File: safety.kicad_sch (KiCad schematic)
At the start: 12 parts, among them J5 Screw_Terminal_01x02, J7 Screw_Terminal_01x02, SW2 SW_DIP_x03, U11 74LVC2G08, U16 74LVC1G175, U17 74HC123, Y2 SG-3031CM

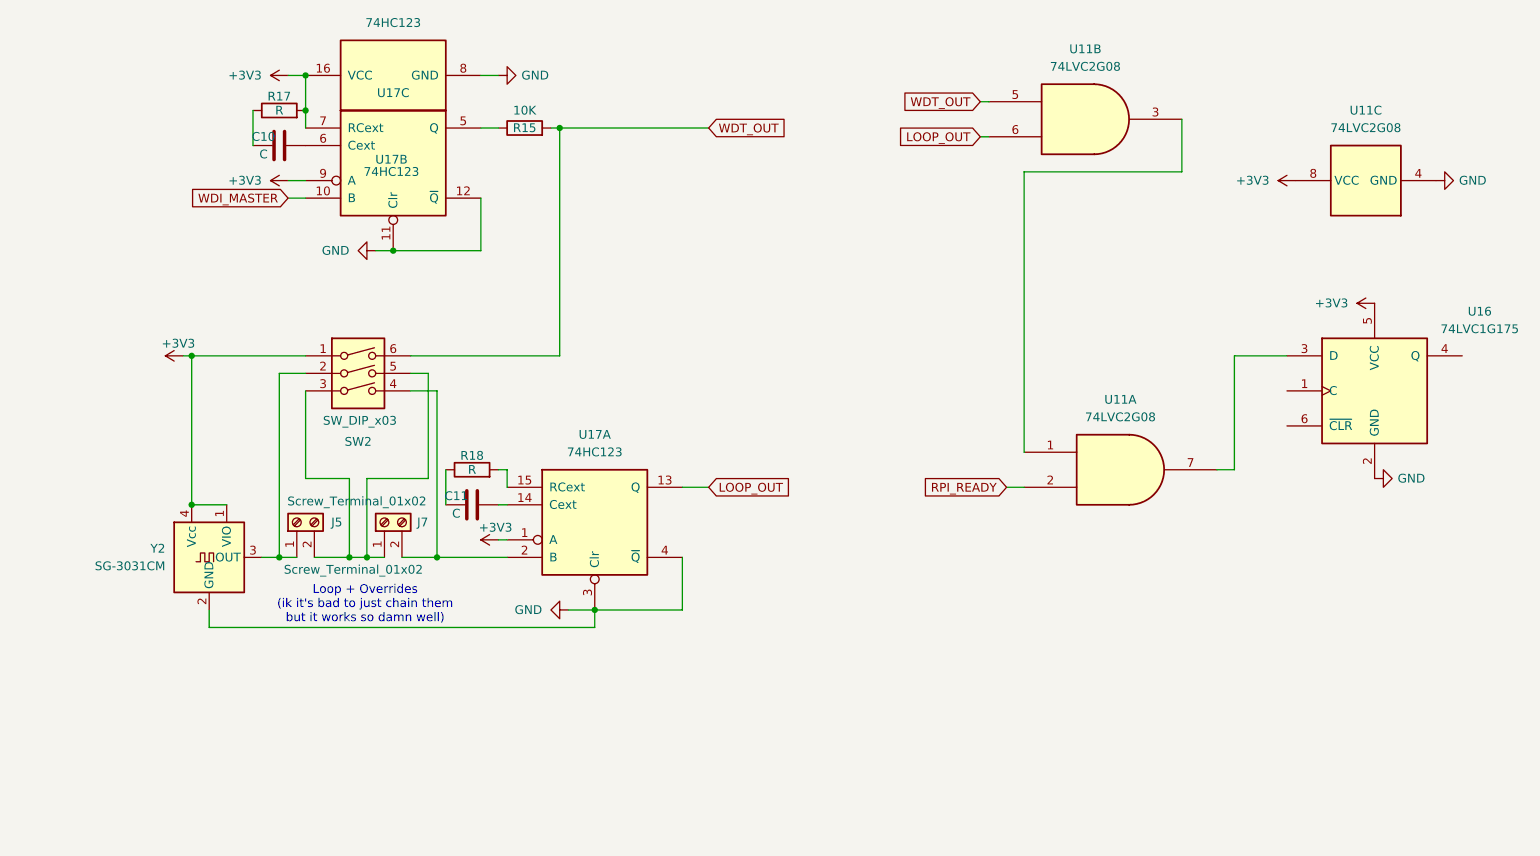
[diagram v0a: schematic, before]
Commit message: Separate safety circuitry, minor schematic changes in main page
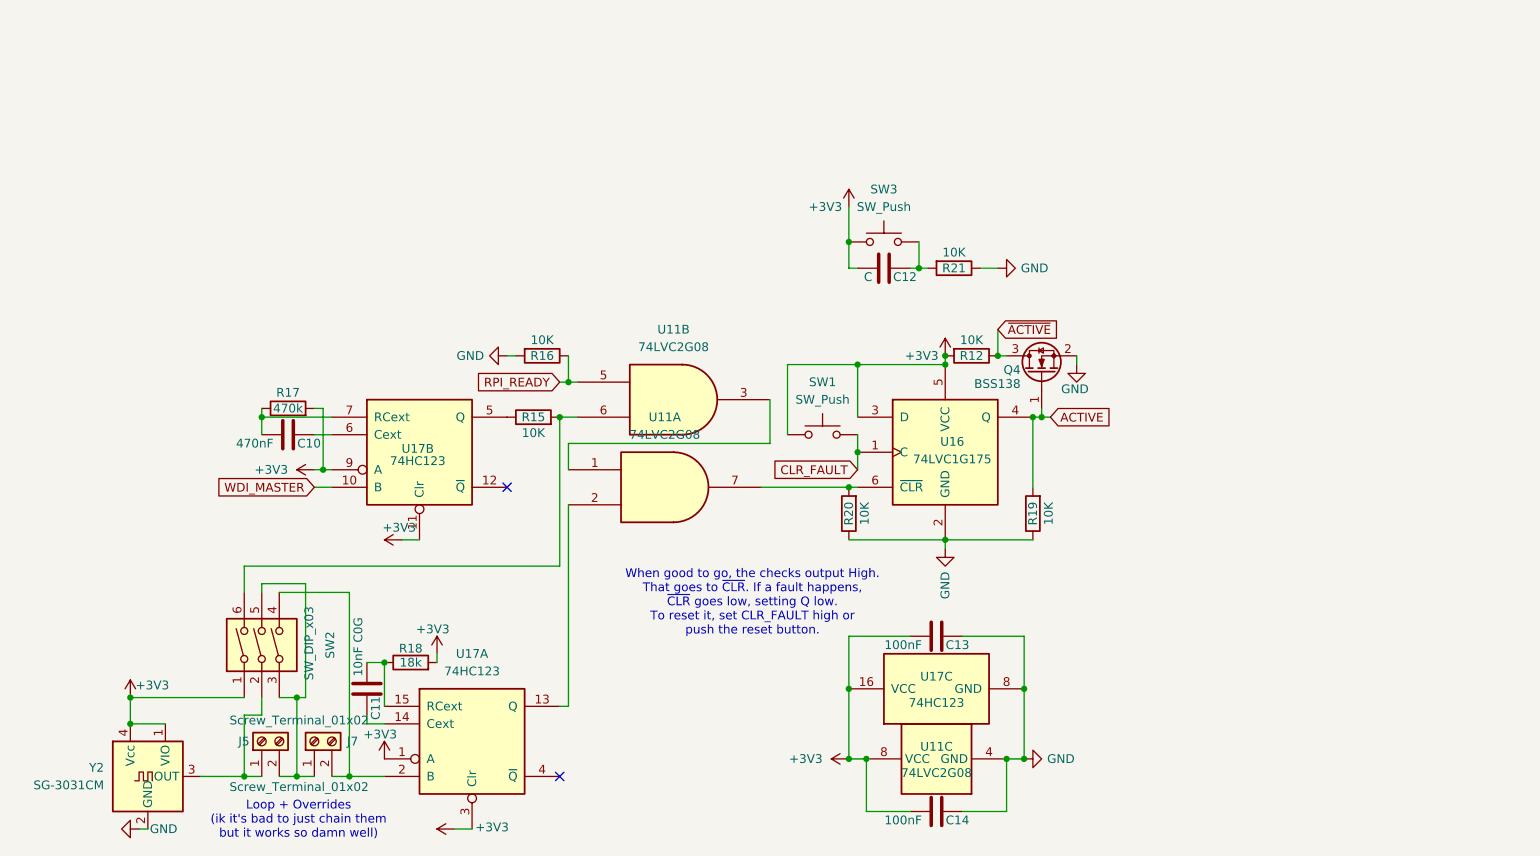
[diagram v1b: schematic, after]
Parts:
- added C12: C, symbol Device:C
- added C13, C14: 100nF, symbol Device:C
- added Q4: BSS138, Package_TO_SOT_SMD:SOT-23, symbol Transistor_FET:BSS138
- added R12, R16, R19, R20, R21: 10K, Resistor_SMD:R_0805_2012Metric_Pad1.20x1.40mm_HandSolder, symbol Device:R
- added SW1, SW3: SW_Push, Button_Switch_SMD:SW_Push_1P1T_NO_CK_KMR2, symbol Switch:SW_Push
- C10: value C -> 470nF
- C11: value C -> 10nF C0G
- R17: value R -> 470k
- R18: value R -> 18k
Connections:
- net +3V3: now also R18.2, U16.3 (D), U17.11 (Clr), U17.3 (Clr), C12.2, C13.2, C14.2, R12.2, SW1.1, SW3.1; no longer U17.7 (RCext)
- net GND: now also C13.1, C14.1, Q4.2 (S), R16.2, R19.1, R20.1, R21.1; no longer U17.11 (Clr), U17.12 (~{Q}), U17.3 (Clr), U17.4 (~{Q})
- net RPI_READY: now also U11.5, R16.1; no longer U11.2
- net at U11.7: now also U16.6 (~{CLR}), R20.2; no longer U16.3 (D)
- net at C11.2, R18.1: now also U17.15 (RCext)
- net at C10.2, R17.1: now also U17.7 (RCext)
- net CLR_FAULT: now reaches U16.1 (C)
- net CLR_FAULT: now also SW1.2
- net ACTIVE: now reaches U16.4 (Q)
- net ACTIVE: now also Q4.1 (G), R19.2
- net LOOP_OUT: no longer names the net of U17.13 (Q)
- net LOOP_OUT: now also U11.2; no longer U11.6
- net WDT_OUT: no longer names the net of R15.2, SW2.6
- net WDT_OUT: now also U11.6; no longer U11.5
- new net: C12.1, R21.2, SW3.2
- new net ~{ACTIVE}: Q4.3 (D), R12.1
- no-connect marks 0 -> 2
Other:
- note added: "When good to go, the checks output High. That goes to ~{CLR}. If a fault happens, ~{CLR} goes low, setting Q low. To reset it, set CLR_FAULT high or push the reset button."
- moved on the sheet: C10, C11, J5, J7, R15, R17, R18, SW2, U11A, U11B, U11C, U16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

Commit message: Started on design, minor touch ups on schematic
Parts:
- removed SW1: SW_Push, Button_Switch_SMD:SW_Push_1P1T_NO_CK_KMR2, symbol Switch:SW_Push
- C10, C11, C13, C14: footprint (none) -> Capacitor_SMD:C_0201_0603Metric_Pad0.64x0.40mm_HandSolder
- C12: value C -> 100nF; footprint (none) -> Capacitor_SMD:C_0201_0603Metric_Pad0.64x0.40mm_HandSolder
- R12, R15, R16, R19, R20, R21: footprint Resistor_SMD:R_0805_2012Metric_Pad1.20x1.40mm_HandSolder -> Resistor_SMD:R_0603_1608Metric_Pad0.98x0.95mm_HandSolder
- R17, R18: footprint (none) -> Resistor_SMD:R_0603_1608Metric_Pad0.98x0.95mm_HandSolder
- U11: footprint (none) -> Package_SO:VSSOP-8_2.3x2mm_P0.5mm
- U17: footprint (none) -> Package_SO:SOP-16_4.4x10.4mm_P1.27mm
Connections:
- net CLR_FAULT: now also C12.1, R21.1, SW3.2
- net GND: now also R21.2; no longer R21.1
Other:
- moved on the sheet: C12, Q4, R12, R19, R20, R21, SW3, U16

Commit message: Did prospective safety circuit design. Terminals are backwards, remember to fix.
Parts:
- SW2: footprint Package_SON:WSON-8-1EP_6x5mm_P1.27mm_EP3.4x4mm -> Button_Switch_SMD:SW_DIP_SPSTx03_Slide_9.78x9.8mm_W8.61mm_P2.54mm
- U16: footprint Relay_THT:Relay_SPDT_Panasonic_DR-L2 -> Package_TO_SOT_SMD:SOT-23-6_Handsoldering
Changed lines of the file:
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@@
 			)
 		)
-		(property "Footprint" "Package_SON:WSON-8-1EP_6x5mm_P1.27mm_EP3.4x4mm"
+		(property "Footprint" "Button_Switch_SMD:SW_DIP_SPSTx03_Slide_9.78x9.8mm_W8.61mm_P2.54mm"
 			(at 106.68 102.87 0)
 			(hide yes)
@@
 			)
 		)
-		(property "Footprint" "Relay_THT:Relay_SPDT_Panasonic_DR-L2"
+		(property "Footprint" "Package_TO_SOT_SMD:SOT-23-6_Handsoldering"
 			(at 205.74 74.93 0)
 			(hide yes)

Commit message: Implementing just so much stuff. RP2350B on board, new sensors, PSU magic, buncha stuff
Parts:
- added JP3: Jumper_2_Bridged, acheron_Connectors:PinHeader_1x2_P2.54mm_Vertical, symbol Jumper:Jumper_2_Bridged
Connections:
- net WDI_MASTER: now also JP3.2 (B); no longer U17.10 (B)
- new net: JP3.1 (A), U17.10 (B)
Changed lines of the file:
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@@
-	(wire
-		(pts
-			(xy 111.76 80.01) (xy 114.3 80.01)
-		)
-		(stroke
-			(width 0)
-			(type default)
-		)
-	)
 	(wire
 		(pts
@@
 		(pts
 			(xy 119.38 114.3) (xy 121.92 114.3)
+		)
+		(stroke
+			(width 0)
+			(type default)
+		)
+	)
+	(wire
+		(pts
+			(xy 102.87 80.01) (xy 104.14 80.01)
 		)
 		(stroke
@@
 	(global_label "WDI_MASTER"
 		(shape input)
-		(at 111.76 80.01 180)
+		(at 102.87 80.01 180)
 		(fields_autoplaced yes)
 		(effects
@@
 		)
 		(property "Intersheetrefs" "${INTERSHEET_REFS}"
-			(at 97.3449 80.01 0)
+			(at 88.4549 80.01 0)
 			(hide yes)
 			(show_name no)
@@
 	(symbol
 		(lib_id "power:+3V3")
-		(at 111.76 77.47 90)
+		(at 111.76 77.47 0)
 		(unit 1)
 		(body_style 1)
@@
 		(in_pos_files yes)
 		(dnp no)
-		(fields_autoplaced yes)
 		(property "Reference" "#PWR070"
-			(at 115.57 77.47 0)
+			(at 111.76 81.28 0)
 			(hide yes)
 			(show_name no)
@@
 		)
 		(property "Value" "+3V3"
-			(at 107.95 77.4699 90)
+			(at 105.41 76.454 0)
 			(show_name no)
 			(do_not_autoplace no)
@@
 				)
 			)
+		)
+	)
+	(symbol
+		(lib_id "Jumper:Jumper_2_Bridged")
+		(at 109.22 80.01 180)
+		(unit 1)
+		(body_style 1)
+		(exclude_from_sim no)
+		(in_bom yes)
+		(on_board yes)
+		(in_pos_files yes)
+		(dnp no)
+		(property "Reference" "JP3"
+			(at 109.22 78.74 0)
+			(show_name no)
+			(do_not_autoplace no)
+			(effects
+				(font
+					(size 1.27 1.27)
+				)
+			)
+		)
+		(property "Value" "Jumper_2_Bridged"
+			(at 109.22 82.042 0)
+			(show_name no)
+			(do_not_autoplace no)
+			(effects
+				(font
+					(size 1.27 1.27)
+				)
+			)
+		)
+		(property "Footprint" "acheron_Connectors:PinHeader_1x2_P2.54mm_Vertical"
+			(at 109.22 80.01 0)
+			(hide yes)
+			(show_name no)
+			(do_not_autoplace no)
+			(effects
+				(font
+					(size 1.27 1.27)
+				)
+			)
+		)
+		(property "Datasheet" ""
+			(at 109.22 74.93 0)
+			(hide yes)
+			(show_name no)
+			(do_not_autoplace no)
+			(effects
+				(font
+					(size 1.27 1.27)
+				)
+			)
+		)
+		(property "Description" "Jumper, 2-pole, closed/bridged"
+			(at 109.22 72.39 0)
+			(hide yes)
+			(show_name no)
+			(do_not_autoplace no)
+			(effects
+				(font
+					(size 1.27 1.27)
+				)
+			)
+		)
+		(pin "1"
+		)
+		(pin "2"
+		)
+		(instances
+			(project "titanRIO"
+				(path "/5914911c-bfc4-448e-a0f4-3ad4bb2a080b/ab83a931-a614-4486-8044-3f1f0e871da9"
+					(reference "JP3")
+					(unit 1)
+				)
+			)

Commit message: Switched back to 2350A, rewired FPGA pins, maybe added some stuff? Idk.
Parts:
- removed R15: 10K, Resistor_SMD:R_0603_1608Metric_Pad0.98x0.95mm_HandSolder, symbol Device:R
- added R26: 10K, Resistor_SMD:R_0603_1608Metric_Pad0.98x0.95mm_HandSolder, symbol Device:R
- C10: footprint Capacitor_SMD:C_0201_0603Metric_Pad0.64x0.40mm_HandSolder -> Capacitor_SMD:C_0603_1608Metric
- C11: footprint Capacitor_SMD:C_0201_0603Metric_Pad0.64x0.40mm_HandSolder -> Capacitor_SMD:C_0603_1608Metric_Pad1.08x0.95mm_HandSolder
- C12, C13, C14: footprint Capacitor_SMD:C_0201_0603Metric_Pad0.64x0.40mm_HandSolder -> Capacitor_SMD:C_0402_1005Metric_Pad0.74x0.62mm_HandSolder
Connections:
- net +3V3: now also JP3.1 (A)
- net WDI_MASTER: now also U17.10 (B); no longer JP3.2 (B)
- net at SW2.6, U11.6: now also U17.5 (Q), R26.1
- new net: JP3.2 (B), R26.2
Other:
- moved on the sheet: JP3, R16
